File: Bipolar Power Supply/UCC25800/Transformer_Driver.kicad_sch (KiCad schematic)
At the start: 24 parts, among them J1 Conn_01x02, T1 750319331, U1 UCC25800

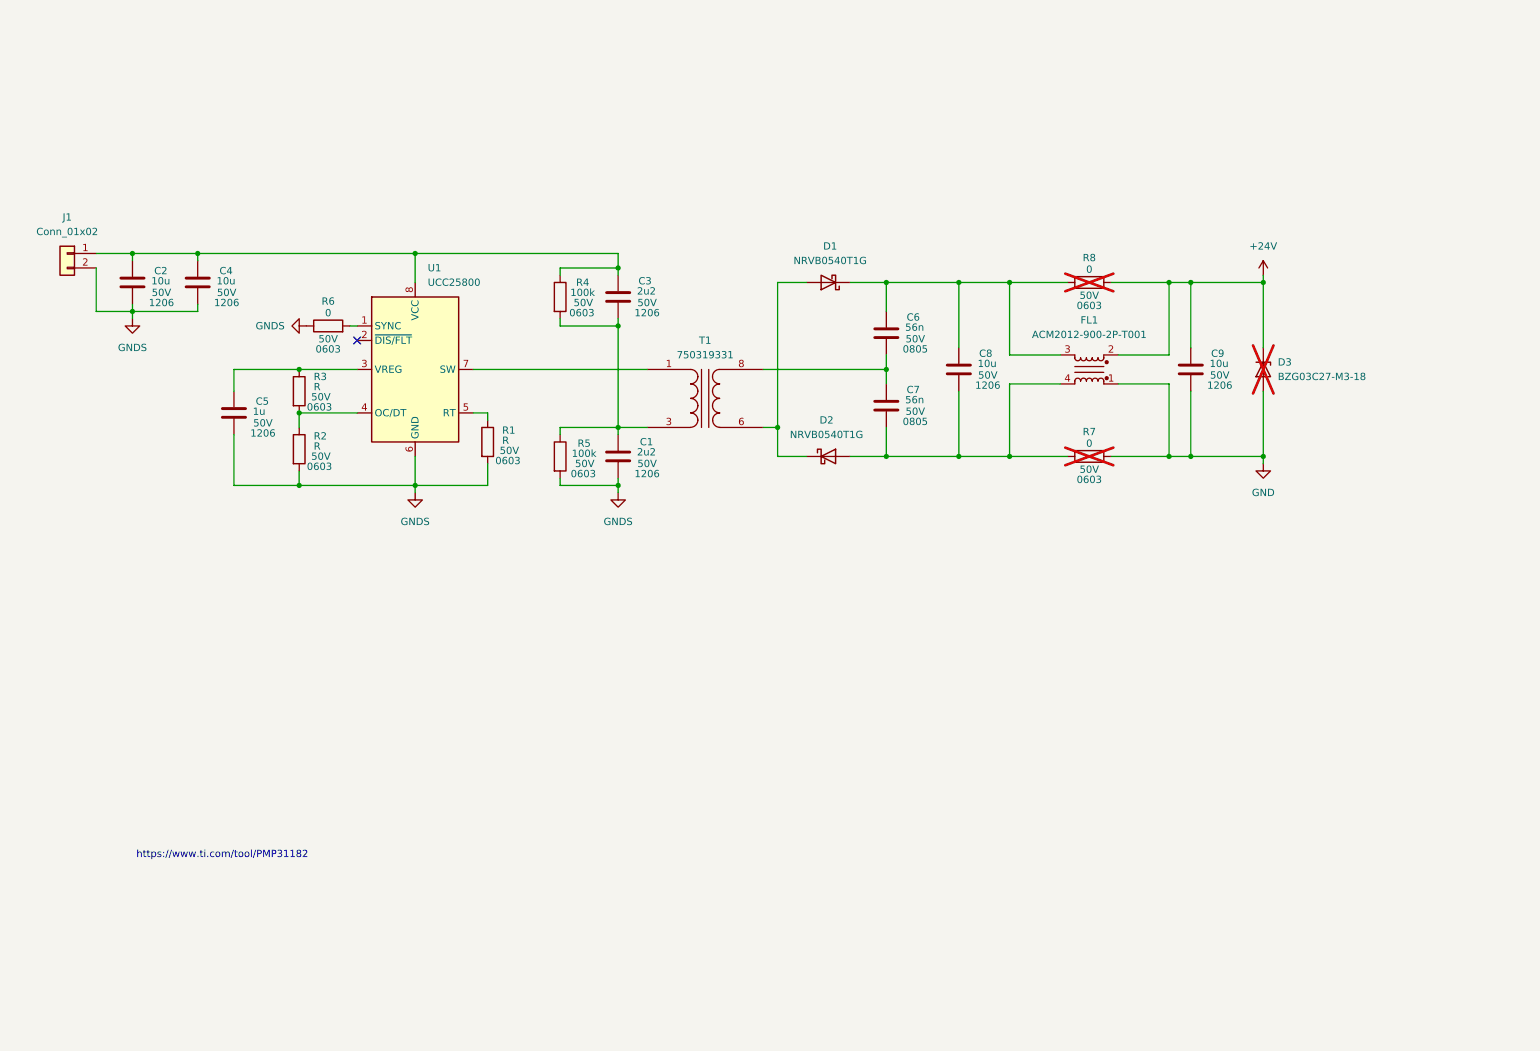
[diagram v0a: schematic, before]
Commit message: UCC25800 : Changes in sch and assignment of footprints.
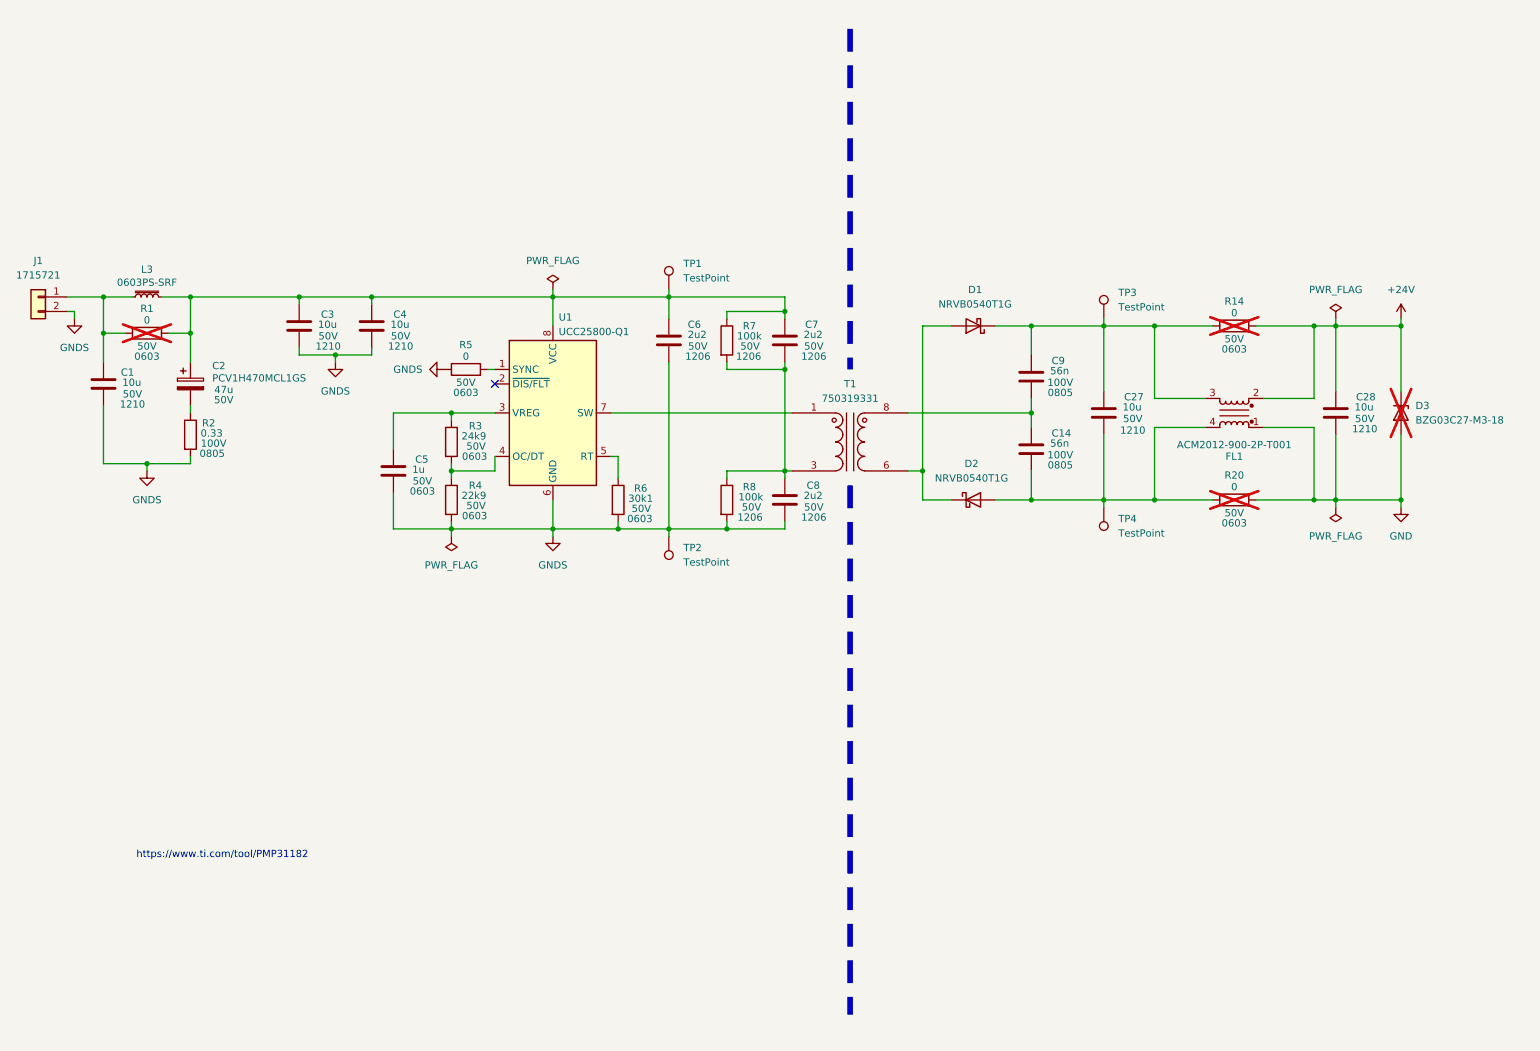
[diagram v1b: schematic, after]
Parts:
- added C1: 10u, Capacitor_SMD:C_1210_3225Metric_Pad1.33x2.70mm_HandSolder, symbol Device:C
- added C2: PCV1H470MCL1GS, Capacitor_SMD:CP_Elec_10x10, symbol Device:C_Polarized
- added C6: 2u2, Capacitor_SMD:C_1206_3216Metric_Pad1.33x1.80mm_HandSolder, symbol Device:C
- added L3: 0603PS-SRF, UCC25800:0603PS-SRF, symbol Device:L_Iron_Small
- added R1: 0, Resistor_SMD:R_0603_1608Metric_Pad0.98x0.95mm_HandSolder, symbol Device:R
- added R2: 0.33, Resistor_SMD:R_0805_2012Metric_Pad1.20x1.40mm_HandSolder, symbol Device:R
- added TP1, TP2, TP3, TP4: TestPoint, TestPoint:TestPoint_Keystone_5005-5009_Compact, symbol Connector:TestPoint
- C14: renamed from C7; footprint (none) -> Capacitor_SMD:C_0805_2012Metric_Pad1.18x1.45mm_HandSolder; Voltage 50V -> 100V
- C27: renamed from C8; footprint (none) -> Capacitor_SMD:C_1210_3225Metric_Pad1.33x2.70mm_HandSolder; Package 1206 -> 1210
- C28: renamed from C9; footprint (none) -> Capacitor_SMD:C_1210_3225Metric_Pad1.33x2.70mm_HandSolder; Package 1206 -> 1210
- C3: renamed from C2; footprint (none) -> Capacitor_SMD:C_1210_3225Metric_Pad1.33x2.70mm_HandSolder; Package 1206 -> 1210
- C4: footprint (none) -> Capacitor_SMD:C_1210_3225Metric_Pad1.33x2.70mm_HandSolder; Package 1206 -> 1210
- C5: footprint (none) -> Capacitor_SMD:C_0603_1608Metric_Pad1.08x0.95mm_HandSolder; Package 1206 -> 0603
- C7: renamed from C3; footprint (none) -> Capacitor_SMD:C_1206_3216Metric_Pad1.33x1.80mm_HandSolder
- C8: renamed from C1; footprint (none) -> Capacitor_SMD:C_1206_3216Metric_Pad1.33x1.80mm_HandSolder
- C9: renamed from C6; footprint (none) -> Capacitor_SMD:C_0805_2012Metric_Pad1.18x1.45mm_HandSolder; Voltage 50V -> 100V
- D1, D2: footprint (none) -> Diode_SMD:D_SOD-123
- D3: footprint (none) -> Diode_SMD:D_SMA
- FL1: footprint Inductor_THT:L_CommonMode_PulseElectronics_PH9455x105NL_1 -> UCC25800:ACM2012-900-2P-T001
- J1: value Conn_01x02 -> 1715721; footprint (none) -> TerminalBlock_Phoenix:TerminalBlock_Phoenix_MKDS-1,5-2_1x02_P5.00mm_Horizontal
- R14: renamed from R8; footprint (none) -> Resistor_SMD:R_0603_1608Metric_Pad0.98x0.95mm_HandSolder; now in the parts list
- R20: renamed from R7; footprint (none) -> Resistor_SMD:R_0603_1608Metric_Pad0.98x0.95mm_HandSolder; now in the parts list
- R3: value R -> 24k9; footprint (none) -> Resistor_SMD:R_0603_1608Metric_Pad0.98x0.95mm_HandSolder
- R4: renamed from R2; value R -> 22k9; footprint (none) -> Resistor_SMD:R_0603_1608Metric_Pad0.98x0.95mm_HandSolder
- R5: renamed from R6; footprint (none) -> Resistor_SMD:R_0603_1608Metric_Pad0.98x0.95mm_HandSolder
- R6: renamed from R1; value R -> 30k1; footprint (none) -> Resistor_SMD:R_0603_1608Metric_Pad0.98x0.95mm_HandSolder
- R7: renamed from R4; footprint (none) -> Resistor_SMD:R_1206_3216Metric_Pad1.30x1.75mm_HandSolder; Package 0603 -> 1206
- R8: renamed from R5; footprint (none) -> Resistor_SMD:R_1206_3216Metric_Pad1.30x1.75mm_HandSolder; Package 0603 -> 1206
- U1: value UCC25800 -> UCC25800-Q1; footprint Package_SO:HVSSOP-8-1EP_3x3mm_P0.65mm_EP1.57x1.89mm -> Package_SO:HVSSOP-8-1EP_3x3mm_P0.65mm_EP1.57x1.89mm_ThermalVias
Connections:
- net GNDS: now also C1.2, C6.2, R2.2, TP2.1
- net at C27.1, C9.1, D1.1 (K)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: now also TP3.1
- net at C14.2, C27.2, D2.2 (A)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: now also TP4.1
- net at C3.1, C4.1, C7.1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: now also C2.1, C6.1, L3.2, R1.2, TP1.1; no longer J1.1 (Pin_1)
- new net: C1.1, J1.1 (Pin_1), L3.1, R1.1
- new net: C2.2, R2.1
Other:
- moved on the sheet: C14, C27, C28, C3, C4, C5, C7, C8, C9, D1, D2, D3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

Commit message: UCC25800 : PCB layout
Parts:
- C6, C7, C8: footprint Capacitor_SMD:C_1206_3216Metric_Pad1.33x1.80mm_HandSolder -> Capacitor_SMD:C_0805_2012Metric_Pad1.18x1.45mm_HandSolder; Package 1206 -> 0805
- R7, R8: footprint Resistor_SMD:R_1206_3216Metric_Pad1.30x1.75mm_HandSolder -> Resistor_SMD:R_0805_2012Metric_Pad1.20x1.40mm_HandSolder; Package 1206 -> 0805
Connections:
- net +24V: now also FL1.1, TP3.1; no longer FL1.2
- net GND: now also FL1.2, TP4.1; no longer FL1.1
- net at C14.2, C27.2, D2.2 (A)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: now also FL1.3; no longer FL1.4, TP4.1
- net at C27.1, C9.1, D1.1 (K)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: now also FL1.4; no longer FL1.3, TP3.1
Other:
- moved on the sheet: FL1, TP3, TP4
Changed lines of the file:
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@@
 		)
 	)
-	(wire
-		(pts
-			(xy 207.01 99.06) (xy 207.01 100.33)
-		)
-		(stroke
-			(width 0)
-			(type default)
-		)
-	)
 	(polyline
 		(pts
@@
 	(wire
 		(pts
+			(xy 259.08 68.58) (xy 260.35 68.58)
+		)
+		(stroke
+			(width 0)
+			(type default)
+		)
+	)
+	(wire
+		(pts
 			(xy 78.74 64.77) (xy 78.74 63.5)
 		)
@@
 	(wire
 		(pts
+			(xy 259.08 99.06) (xy 260.35 99.06)
+		)
+		(stroke
+			(width 0)
+			(type default)
+		)
+	)
+	(wire
+		(pts
 			(xy 121.92 104.14) (xy 130.81 104.14)
 		)
@@
 	(wire
 		(pts
-			(xy 207.01 67.31) (xy 207.01 68.58)
-		)
-		(stroke
-			(width 0)
-			(type default)
-		)
-	)
-	(wire
-		(pts
 			(xy 247.65 99.06) (xy 259.08 99.06)
 		)
@@
 	(symbol
 		(lib_id "Connector:TestPoint")
-		(at 207.01 100.33 180)
+		(at 260.35 99.06 270)
 		(unit 1)
 		(exclude_from_sim no)
@@
 		(fields_autoplaced yes)
 		(property "Reference" "TP4"
-			(at 209.55 102.3619 0)
+			(at 265.43 97.7899 90)
 			(effects
 				(font
 					(size 1.27 1.27)
 				)
-				(justify right)
+				(justify left)
 			)
 		)
 		(property "Value" "TestPoint"
-			(at 209.55 104.9019 0)
+			(at 265.43 100.3299 90)
 			(effects
 				(font
 					(size 1.27 1.27)
 				)
-				(justify right)
+				(justify left)
 			)
 		)
 		(property "Footprint" "TestPoint:TestPoint_Keystone_5005-5009_Compact"
-			(at 201.93 100.33 0)
+			(at 260.35 104.14 0)
 			(effects
 				(font
@@
 		)
 		(property "Datasheet" "~"
-			(at 201.93 100.33 0)
+			(at 260.35 104.14 0)
 			(effects
 				(font
@@
 		)
 		(property "Description" "test point"
-			(at 207.01 100.33 0)
+			(at 260.35 99.06 0)
 			(effects
 				(font
@@
 	(symbol
 		(lib_id "Filter:Choke_CommonMode_PulseElectronics_PH9455x105NL")
-		(at 229.87 83.82 180)
+		(at 229.87 83.82 0)
+		(mirror y)
 		(unit 1)
 		(exclude_from_sim no)
@@
 		(dnp no)
 		(property "Reference" "FL1"
-			(at 229.87 91.44 0)
+			(at 229.87 76.2 0)
 			(effects
 				(font
@@
 		)
 		(property "Value" "ACM2012-900-2P-T001"
-			(at 229.87 89.408 0)
+			(at 229.87 78.232 0)
 			(effects
 				(font
@@
 			)
 		)
-		(property "Footprint" "Resistor_SMD:R_1206_3216Metric_Pad1.30x1.75mm_HandSolder"
+		(property "Footprint" "Resistor_SMD:R_0805_2012Metric_Pad1.20x1.40mm_HandSolder"
 			(at 139.192 99.06 90)
 			(effects
@@
 			)
 		)
-		(property "Package" "1206"
+		(property "Package" "0805"
 			(at 145.034 102.108 0)
 			(effects
@@
 	(symbol
 		(lib_id "Connector:TestPoint")
-		(at 207.01 67.31 0)
+		(at 260.35 68.58 270)
 		(unit 1)
 		(exclude_from_sim no)
@@
 		(fields_autoplaced yes)
 		(property "Reference" "TP3"
-			(at 209.55 62.7379 0)
+			(at 265.43 67.3099 90)
 			(effects
 				(font
@@
 		)
 		(property "Value" "TestPoint"
-			(at 209.55 65.2779 0)
+			(at 265.43 69.8499 90)
 			(effects
 				(font
@@
 		)
 		(property "Footprint" "TestPoint:TestPoint_Keystone_5005-5009_Compact"
-			(at 212.09 67.31 0)
+			(at 260.35 73.66 0)
 			(effects
 				(font
@@
 		)
 		(property "Datasheet" "~"
-			(at 212.09 67.31 0)
+			(at 260.35 73.66 0)
 			(effects
 				(font
@@
 		)
 		(property "Description" "test point"
-			(at 207.01 67.31 0)
+			(at 260.35 68.58 0)
 			(effects
 				(font
@@
 			)
 		)
-		(property "Footprint" "Capacitor_SMD:C_1206_3216Metric_Pad1.33x1.80mm_HandSolder"
+		(property "Footprint" "Capacitor_SMD:C_0805_2012Metric_Pad1.18x1.45mm_HandSolder"
 			(at 131.7752 74.93 0)
 			(effects
@@
 			)
 		)
-		(property "Package" "1206"
+		(property "Package" "0805"
 			(at 135.89 73.914 0)
 			(effects
@@
 			)
 		)
-		(property "Footprint" "Resistor_SMD:R_1206_3216Metric_Pad1.30x1.75mm_HandSolder"
+		(property "Footprint" "Resistor_SMD:R_0805_2012Metric_Pad1.20x1.40mm_HandSolder"
 			(at 139.192 71.12 90)
 			(effects
@@
 			)
 		)
-		(property "Package" "1206"
+		(property "Package" "0805"
 			(at 144.78 73.914 0)
 			(effects
@@
 			)
 		)
-		(property "Footprint" "Capacitor_SMD:C_1206_3216Metric_Pad1.33x1.80mm_HandSolder"
+		(property "Footprint" "Capacitor_SMD:C_0805_2012Metric_Pad1.18x1.45mm_HandSolder"
 			(at 152.0952 74.93 0)
 			(effects
@@
 			)
 		)
-		(property "Package" "1206"
+		(property "Package" "0805"
 			(at 156.21 73.914 0)
 			(effects
@@
 			)
 		)
-		(property "Footprint" "Capacitor_SMD:C_1206_3216Metric_Pad1.33x1.80mm_HandSolder"
+		(property "Footprint" "Capacitor_SMD:C_0805_2012Metric_Pad1.18x1.45mm_HandSolder"
 			(at 152.0952 102.87 0)
 			(effects
@@
 			)
 		)
-		(property "Package" "1206"
+		(property "Package" "0805"
 			(at 156.21 102.108 0)
 			(effects
